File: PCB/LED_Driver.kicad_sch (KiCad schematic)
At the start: 8 parts, among them J1 Conn_Coaxial_Power, J4 Conn_01x04_Male, J5 Screw_Terminal_01x05, Q1 IRLB8721PBF, Q2 IRLB8721PBF, Q3 IRLB8721PBF, Q4 IRLB8721PBF, U1 ESP32_DevKit_V1_DOIT

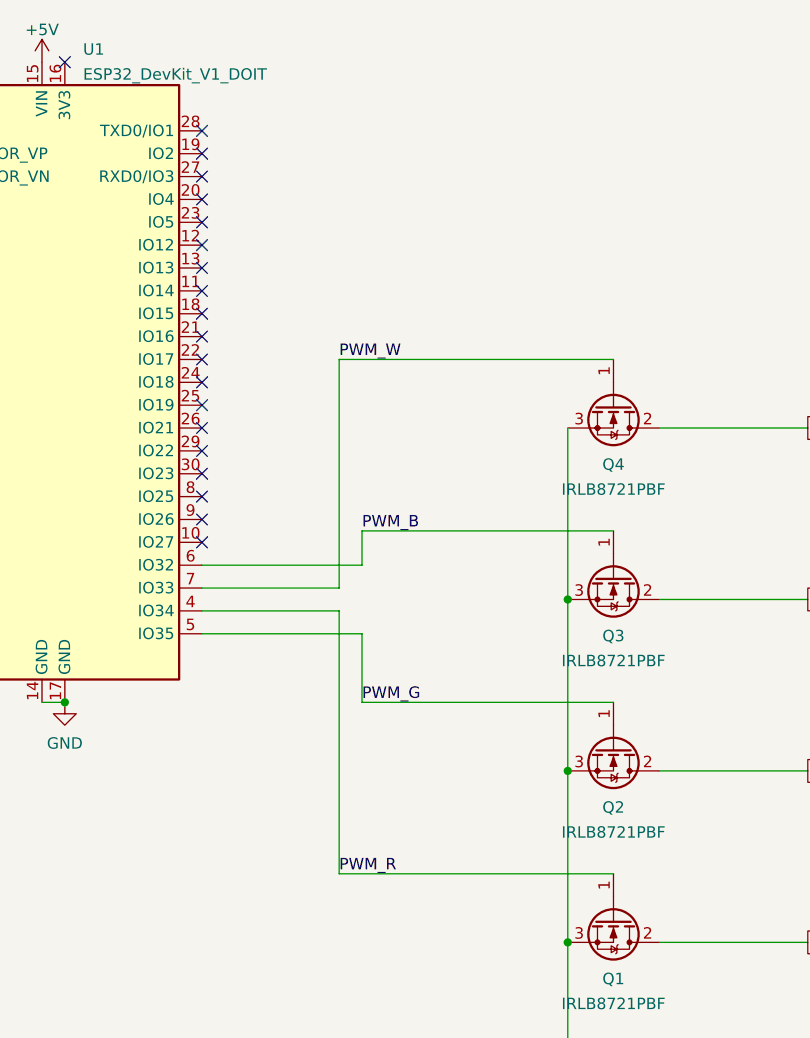
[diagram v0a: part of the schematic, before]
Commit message: Updates the connections to the ESP32. The original pins were input only pins, according to esphome
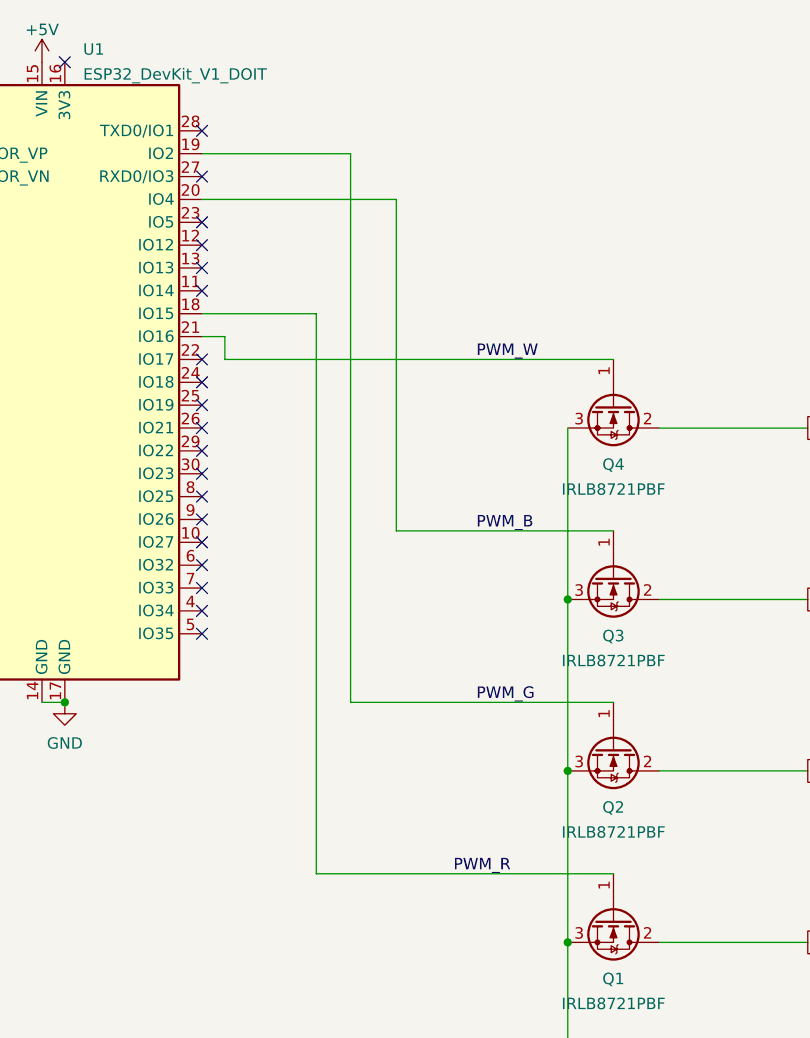
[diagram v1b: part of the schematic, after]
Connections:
- net PWM_B: now also U1.20 (IO4); no longer U1.6 (IO32)
- net PWM_G: now also U1.19 (IO2); no longer U1.5 (IO35)
- net PWM_R: now also U1.18 (IO15); no longer U1.4 (IO34)
- net PWM_W: now also U1.21 (IO16); no longer U1.7 (IO33)
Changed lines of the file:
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@@
   (no_connect (at 87.63 59.69))
   (no_connect (at 87.63 57.15))
-  (no_connect (at 87.63 39.37))
+  (no_connect (at 87.63 82.55))
   (no_connect (at 87.63 46.99))
   (no_connect (at 72.39 24.13))
@@
   (no_connect (at 87.63 31.75))
   (no_connect (at 87.63 44.45))
-  (no_connect (at 87.63 34.29))
+  (no_connect (at 87.63 80.01))
   (no_connect (at 87.63 36.83))
-  (no_connect (at 87.63 52.07))
+  (no_connect (at 87.63 85.09))
   (no_connect (at 87.63 41.91))
   (no_connect (at 87.63 74.93))
@@
   (no_connect (at 87.63 62.23))
   (no_connect (at 87.63 77.47))
-  (no_connect (at 87.63 54.61))
+  (no_connect (at 87.63 87.63))
   (wire (pts (xy 99.06 153.67) (xy 99.06 156.21))
-    (stroke (width 0) (type default) (color 0 0 0 0))
-  )
-  (wire (pts (xy 102.87 85.09) (xy 87.63 85.09))
     (stroke (width 0) (type default) (color 0 0 0 0))
   )
@@
     (stroke (width 0) (type default) (color 0 0 0 0))
   )
-  (wire (pts (xy 102.87 114.3) (xy 102.87 85.09))
+  (wire (pts (xy 109.22 39.37) (xy 87.63 39.37))
     (stroke (width 0) (type default) (color 0 0 0 0))
   )
@@
     (stroke (width 0) (type default) (color 0 0 0 0))
   )
+  (wire (pts (xy 109.22 76.2) (xy 109.22 39.37))
+    (stroke (width 0) (type default) (color 0 0 0 0))
+  )
+  (wire (pts (xy 90.17 57.15) (xy 90.17 54.61))
+    (stroke (width 0) (type default) (color 0 0 0 0))
+  )
   (wire (pts (xy 35.56 151.13) (xy 40.64 151.13))
+    (stroke (width 0) (type default) (color 0 0 0 0))
+  )
+  (wire (pts (xy 90.17 57.15) (xy 133.35 57.15))
     (stroke (width 0) (type default) (color 0 0 0 0))
   )
@@
     (stroke (width 0) (type default) (color 0 0 0 0))
   )
-  (wire (pts (xy 87.63 80.01) (xy 105.41 80.01))
+  (wire (pts (xy 104.14 95.25) (xy 104.14 34.29))
+    (stroke (width 0) (type default) (color 0 0 0 0))
+  )
+  (wire (pts (xy 100.33 52.07) (xy 87.63 52.07))
     (stroke (width 0) (type default) (color 0 0 0 0))
   )
@@
     (stroke (width 0) (type default) (color 0 0 0 0))
   )
-  (wire (pts (xy 87.63 87.63) (xy 105.41 87.63))
-    (stroke (width 0) (type default) (color 0 0 0 0))
-  )
   (wire (pts (xy 40.64 151.13) (xy 43.18 151.13))
     (stroke (width 0) (type default) (color 0 0 0 0))
@@
     (stroke (width 0) (type default) (color 0 0 0 0))
   )
-  (wire (pts (xy 133.35 95.25) (xy 105.41 95.25))
-    (stroke (width 0) (type default) (color 0 0 0 0))
-  )
-  (wire (pts (xy 102.87 57.15) (xy 102.87 82.55))
+  (wire (pts (xy 104.14 95.25) (xy 133.35 95.25))
     (stroke (width 0) (type default) (color 0 0 0 0))
   )
@@
     (stroke (width 0) (type default) (color 0 0 0 0))
   )
-  (wire (pts (xy 133.35 57.15) (xy 102.87 57.15))
-    (stroke (width 0) (type default) (color 0 0 0 0))
-  )
-  (wire (pts (xy 133.35 76.2) (xy 105.41 76.2))
-    (stroke (width 0) (type default) (color 0 0 0 0))
-  )
-  (wire (pts (xy 105.41 76.2) (xy 105.41 80.01))
+  (wire (pts (xy 109.22 76.2) (xy 133.35 76.2))
     (stroke (width 0) (type default) (color 0 0 0 0))
   )
@@
     (stroke (width 0) (type default) (color 0 0 0 0))
   )
-  (wire (pts (xy 102.87 82.55) (xy 87.63 82.55))
+  (wire (pts (xy 90.17 54.61) (xy 87.63 54.61))
     (stroke (width 0) (type default) (color 0 0 0 0))
   )
-  (wire (pts (xy 105.41 95.25) (xy 105.41 87.63))
+  (wire (pts (xy 100.33 114.3) (xy 100.33 52.07))
     (stroke (width 0) (type default) (color 0 0 0 0))
   )
@@
     (stroke (width 0) (type default) (color 0 0 0 0))
   )
-  (wire (pts (xy 133.35 114.3) (xy 102.87 114.3))
+  (wire (pts (xy 104.14 34.29) (xy 87.63 34.29))
+    (stroke (width 0) (type default) (color 0 0 0 0))
+  )
+  (wire (pts (xy 100.33 114.3) (xy 133.35 114.3))
     (stroke (width 0) (type default) (color 0 0 0 0))
   )
@@
     (stroke (width 0) (type default) (color 0 0 0 0))
   )
-  (label "PWM_R" (at 102.87 114.3 0)
+  (label "PWM_R" (at 115.57 114.3 0)
     (effects (font (size 1.27 1.27)) (justify left bottom))
   )
-  (label "PWM_G" (at 105.41 95.25 0)
+  (label "PWM_G" (at 118.11 95.25 0)
     (effects (font (size 1.27 1.27)) (justify left bottom))
   )
-  (label "PWM_B" (at 105.41 76.2 0)
+  (label "PWM_B" (at 118.11 76.2 0)
     (effects (font (size 1.27 1.27)) (justify left bottom))
   )
-  (label "PWM_W" (at 102.87 57.15 0)
+  (label "PWM_W" (at 118.11 57.15 0)
     (effects (font (size 1.27 1.27)) (justify left bottom))
   )

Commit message: Makes board smaller using proper terminal blocks
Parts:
- removed J5: Screw_Terminal_01x05, Connector_Phoenix_MSTB:PhoenixContact_MSTBA_2,5_5-G_1x05_P5.00mm_Horizontal, symbol Connector:Screw_Terminal_01x05
- added J2: Screw_Terminal_01x06, TerminalBlock:TerminalBlock_bornier-6_P5.08mm, symbol Connector:Screw_Terminal_01x06
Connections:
- net +12V: now also J2.5 (Pin_5), J2.6 (Pin_6)
- net LED_B: now also J2.3 (Pin_3)
- net LED_G: now also J2.2 (Pin_2)
- net LED_R: now also J2.1 (Pin_1)
- net LED_W: now also J2.4 (Pin_4)
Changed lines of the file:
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@@
   (junction (at 128.27 121.92) (diameter 0) (color 0 0 0 0)
+  )
+  (junction (at 220.98 100.33) (diameter 0) (color 0 0 0 0)
   )
   (junction (at 92.71 158.75) (diameter 0) (color 0 0 0 0)
@@
     (stroke (width 0) (type default) (color 0 0 0 0))
   )
+  (wire (pts (xy 220.98 100.33) (xy 220.98 102.87))
+    (stroke (width 0) (type default) (color 0 0 0 0))
+  )
   (wire (pts (xy 100.33 114.3) (xy 100.33 52.07))
     (stroke (width 0) (type default) (color 0 0 0 0))
@@
     (pin "2")
     (pin "3")
-  )
-  (symbol (lib_id "Connector:Screw_Terminal_01x05") (at 226.06 95.25 0) (unit 1)
-    (in_bom yes) (on_board yes) (fields_autoplaced)
-    (property "Reference" "J5" (id 0) (at 228.092 94.3415 0)
-      (effects (font (size 1.27 1.27)) (justify left))
-    )
-    (property "Value" "Screw_Terminal_01x05" (id 1) (at 228.092 97.1166 0)
-      (effects (font (size 1.27 1.27)) (justify left))
-    )
-    (property "Footprint" "Connector_Phoenix_MSTB:PhoenixContact_MSTBA_2,5_5-G_1x05_P5.00mm_Horizontal" (id 2) (at 226.06 95.25 0)
-      (effects (font (size 1.27 1.27)) hide)
-    )
-    (property "Datasheet" "~" (id 3) (at 226.06 95.25 0)
-      (effects (font (size 1.27 1.27)) hide)
-    )
-    (pin "1")
-    (pin "2")
-    (pin "3")
-    (pin "4")
-    (pin "5")
   )
   (symbol (lib_id "power:GND") (at 72.39 95.25 0) (mirror y) (unit 1)
@@
     (pin "1")
   )
+  (symbol (lib_id "Connector:Screw_Terminal_01x06") (at 226.06 95.25 0) (unit 1)
+    (in_bom yes) (on_board yes) (fields_autoplaced)
+    (property "Reference" "J2" (id 0) (at 228.092 95.6115 0)
+      (effects (font (size 1.27 1.27)) (justify left))
+    )
+    (property "Value" "Screw_Terminal_01x06" (id 1) (at 228.092 98.3866 0)
+      (effects (font (size 1.27 1.27)) (justify left))
+    )
+    (property "Footprint" "TerminalBlock:TerminalBlock_bornier-6_P5.08mm" (id 2) (at 226.06 95.25 0)
+      (effects (font (size 1.27 1.27)) hide)
+    )
+    (property "Datasheet" "~" (id 3) (at 226.06 95.25 0)
+      (effects (font (size 1.27 1.27)) hide)
+    )
+    (pin "1")
+    (pin "2")
+    (pin "3")
+    (pin "4")
+    (pin "5")
+    (pin "6")
+  )
   (symbol (lib_id "power:+12V") (at 87.63 156.21 90) (unit 1)
     (in_bom yes) (on_board yes) (fields_autoplaced)
@@
       (reference "J1") (unit 1) (value "Conn_Coaxial_Power") (footprint "Connector_BarrelJack:BarrelJack_Horizontal")
     )
+    (path "/7fa8a569-0450-4b0c-984a-257661b17cdb"
+      (reference "J2") (unit 1) (value "Screw_Terminal_01x06") (footprint "TerminalBlock:TerminalBlock_bornier-6_P5.08mm")
+    )
     (path "/22b26b6d-47c9-4306-8d3a-7de2e7b5a3f8"
       (reference "J4") (unit 1) (value "Conn_01x04_Male") (footprint "Connector_PinHeader_2.54mm:PinHeader_1x04_P2.54mm_Vertical")
     )
-    (path "/4ffa21c6-57d0-49e1-a200-5f92c1bd994a"
-      (reference "J5") (unit 1) (value "Screw_Terminal_01x05") (footprint "Connector_Phoenix_MSTB:PhoenixContact_MSTBA_2,5_5-G_1x05_P5.00mm_Horizontal")
-    )
     (path "/22999e73-da32-43a5-9163-4b3a41614f25"

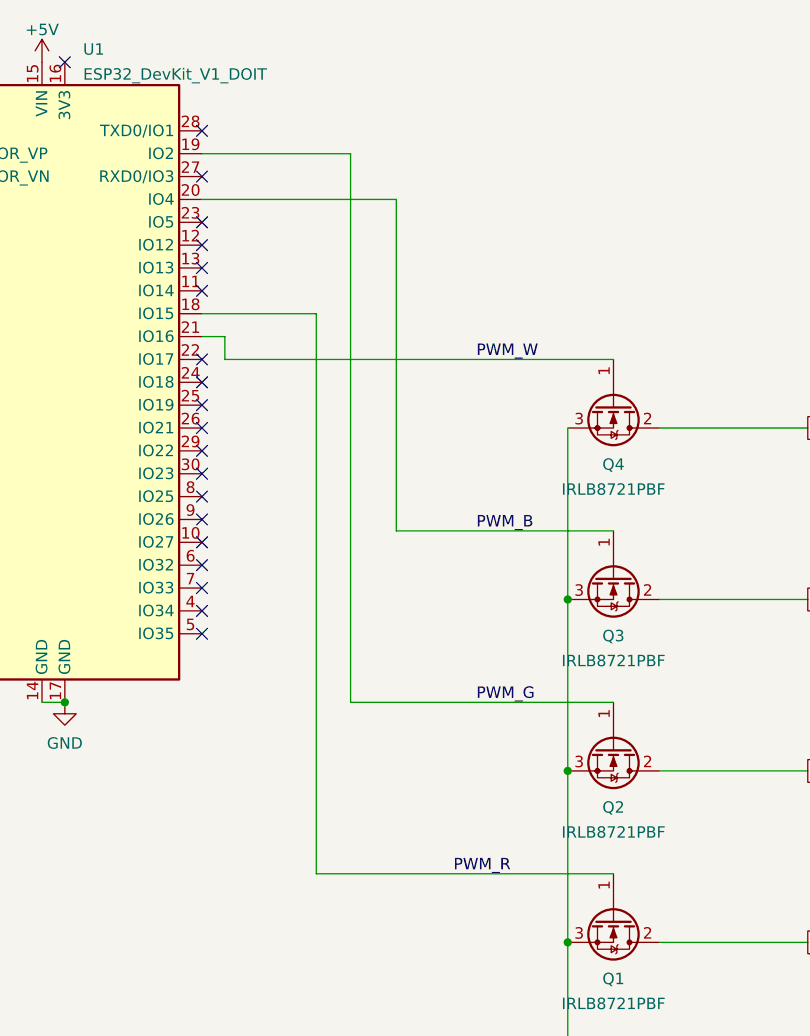
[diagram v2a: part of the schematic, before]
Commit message: Updates pins that are driving gates of transistors. 3 of the original ones were strapping pins on the esp32
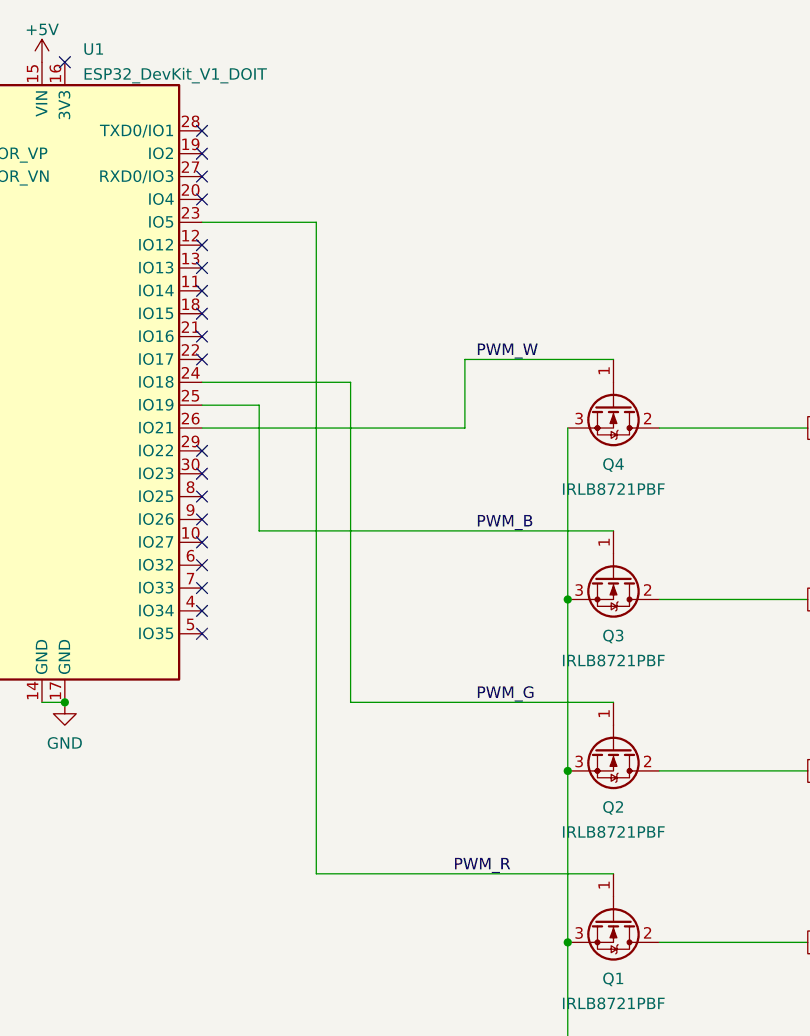
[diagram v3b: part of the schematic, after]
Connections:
- net PWM_B: now also U1.25 (IO19); no longer U1.20 (IO4)
- net PWM_G: now also U1.24 (IO18); no longer U1.19 (IO2)
- net PWM_R: now also U1.23 (IO5); no longer U1.18 (IO15)
- net PWM_W: now also U1.26 (IO21); no longer U1.21 (IO16)
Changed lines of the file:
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@@
   (junction (at 99.06 156.21) (diameter 0) (color 0 0 0 0)
   )
-  (no_connect (at 87.63 59.69))
+  (no_connect (at 87.63 34.29))
   (no_connect (at 87.63 57.15))
   (no_connect (at 87.63 82.55))
@@
   (no_connect (at 87.63 36.83))
   (no_connect (at 87.63 85.09))
-  (no_connect (at 87.63 41.91))
+  (no_connect (at 87.63 52.07))
   (no_connect (at 87.63 74.93))
   (no_connect (at 87.63 72.39))
   (no_connect (at 87.63 69.85))
   (no_connect (at 87.63 67.31))
-  (no_connect (at 87.63 64.77))
-  (no_connect (at 87.63 62.23))
+  (no_connect (at 87.63 54.61))
+  (no_connect (at 87.63 39.37))
   (no_connect (at 87.63 77.47))
   (no_connect (at 87.63 87.63))
@@
     (stroke (width 0) (type default) (color 0 0 0 0))
   )
-  (wire (pts (xy 128.27 102.87) (xy 128.27 121.92))
+  (wire (pts (xy 133.35 57.15) (xy 116.84 57.15))
     (stroke (width 0) (type default) (color 0 0 0 0))
   )
-  (wire (pts (xy 109.22 39.37) (xy 87.63 39.37))
+  (wire (pts (xy 128.27 102.87) (xy 128.27 121.92))
     (stroke (width 0) (type default) (color 0 0 0 0))
   )
@@
     (stroke (width 0) (type default) (color 0 0 0 0))
   )
-  (wire (pts (xy 109.22 76.2) (xy 109.22 39.37))
-    (stroke (width 0) (type default) (color 0 0 0 0))
-  )
-  (wire (pts (xy 90.17 57.15) (xy 90.17 54.61))
-    (stroke (width 0) (type default) (color 0 0 0 0))
-  )
   (wire (pts (xy 35.56 151.13) (xy 40.64 151.13))
     (stroke (width 0) (type default) (color 0 0 0 0))
   )
-  (wire (pts (xy 90.17 57.15) (xy 133.35 57.15))
+  (wire (pts (xy 116.84 64.77) (xy 87.63 64.77))
     (stroke (width 0) (type default) (color 0 0 0 0))
   )
@@
     (stroke (width 0) (type default) (color 0 0 0 0))
   )
-  (wire (pts (xy 104.14 95.25) (xy 104.14 34.29))
-    (stroke (width 0) (type default) (color 0 0 0 0))
-  )
-  (wire (pts (xy 100.33 52.07) (xy 87.63 52.07))
+  (wire (pts (xy 87.63 59.69) (xy 104.14 59.69))
     (stroke (width 0) (type default) (color 0 0 0 0))
   )
@@
     (stroke (width 0) (type default) (color 0 0 0 0))
   )
+  (wire (pts (xy 93.98 76.2) (xy 93.98 62.23))
+    (stroke (width 0) (type default) (color 0 0 0 0))
+  )
+  (wire (pts (xy 87.63 41.91) (xy 100.33 41.91))
+    (stroke (width 0) (type default) (color 0 0 0 0))
+  )
   (wire (pts (xy 87.63 156.21) (xy 99.06 156.21))
+    (stroke (width 0) (type default) (color 0 0 0 0))
+  )
+  (wire (pts (xy 100.33 41.91) (xy 100.33 114.3))
+    (stroke (width 0) (type default) (color 0 0 0 0))
+  )
+  (wire (pts (xy 104.14 59.69) (xy 104.14 95.25))
     (stroke (width 0) (type default) (color 0 0 0 0))
   )
@@
     (stroke (width 0) (type default) (color 0 0 0 0))
   )
+  (wire (pts (xy 93.98 62.23) (xy 87.63 62.23))
+    (stroke (width 0) (type default) (color 0 0 0 0))
+  )
   (wire (pts (xy 138.43 83.82) (xy 154.94 83.82))
     (stroke (width 0) (type default) (color 0 0 0 0))
   )
-  (wire (pts (xy 109.22 76.2) (xy 133.35 76.2))
+  (wire (pts (xy 93.98 76.2) (xy 133.35 76.2))
     (stroke (width 0) (type default) (color 0 0 0 0))
   )
@@
     (stroke (width 0) (type default) (color 0 0 0 0))
   )
-  (wire (pts (xy 90.17 54.61) (xy 87.63 54.61))
-    (stroke (width 0) (type default) (color 0 0 0 0))
-  )
   (wire (pts (xy 220.98 100.33) (xy 220.98 102.87))
-    (stroke (width 0) (type default) (color 0 0 0 0))
-  )
-  (wire (pts (xy 100.33 114.3) (xy 100.33 52.07))
     (stroke (width 0) (type default) (color 0 0 0 0))
   )
@@
     (stroke (width 0) (type default) (color 0 0 0 0))
   )
-  (wire (pts (xy 104.14 34.29) (xy 87.63 34.29))
+  (wire (pts (xy 116.84 57.15) (xy 116.84 64.77))
     (stroke (width 0) (type default) (color 0 0 0 0))
   )
